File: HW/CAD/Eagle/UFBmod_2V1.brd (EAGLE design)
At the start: 98.4 x 89.5 mm, 204 parts, among them J1411 ABRACON_ARJE-0034, T0551 MMBT2222, U0501 MIDAS_MCCOG21605B6W-FPTLWI, U0601 MAX5217, U0701 AT86RF215-ZU, U0711 ASVTX-13-D-26.000MHZ-I05-T, U0811 PE4259, U0821 RFX1010, U0881 B39871B3440U410, U0911 FT232HL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

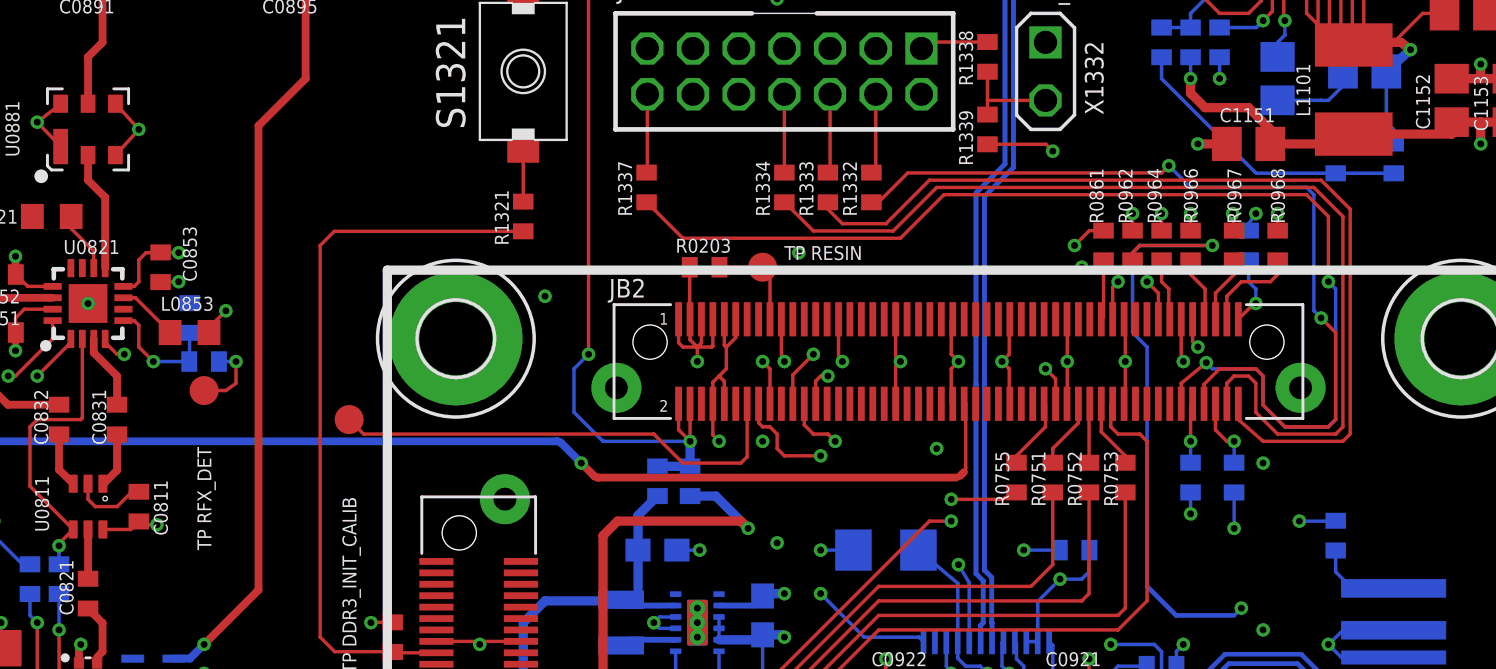
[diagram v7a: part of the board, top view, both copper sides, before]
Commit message: HW_2V1 - CAD/Eagle - missing polygone isles connected
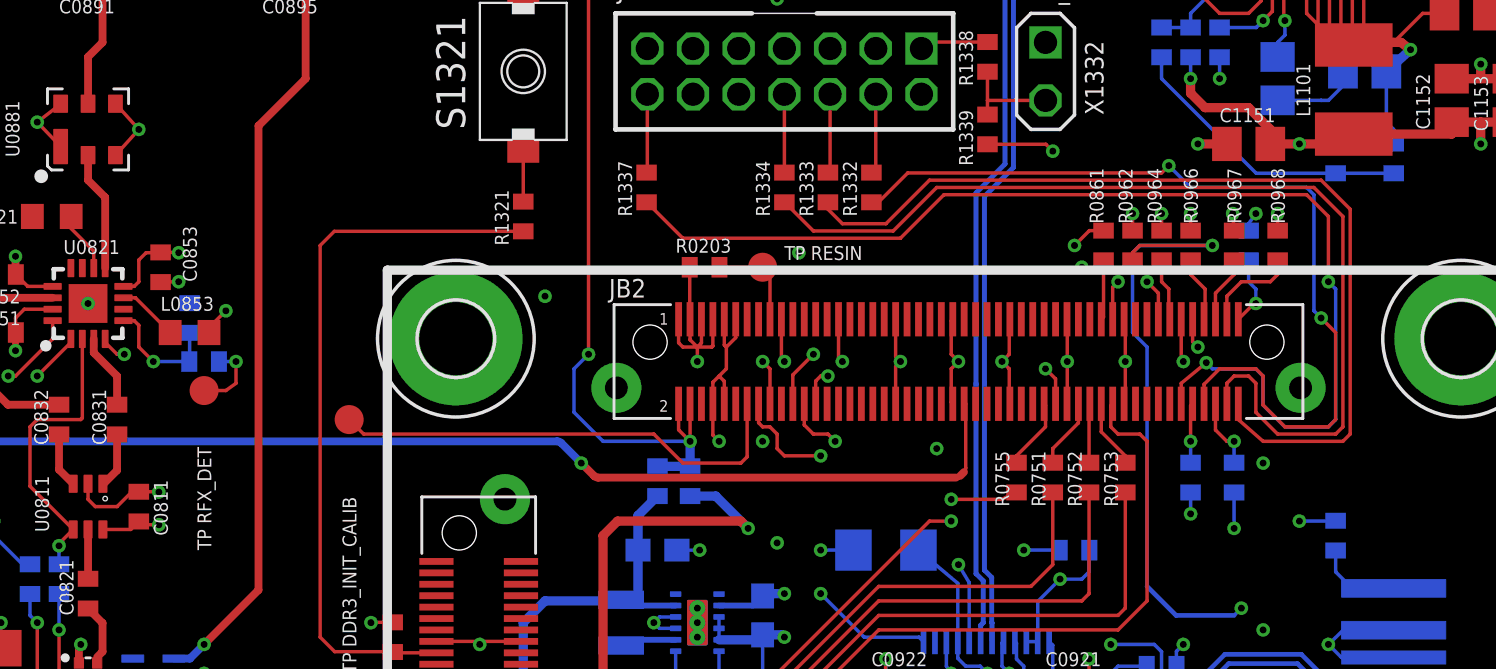
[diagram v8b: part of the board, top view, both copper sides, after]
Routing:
- net +3V3: track 98.2 -> 125.0 mm, vias 21 -> 22
- net GND: track 241.2 -> 242.1 mm, vias 83 -> 84
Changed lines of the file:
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@@
 <layer number="21" name="tPlace" color="7" fill="1" visible="yes" active="yes"/>
 <layer number="22" name="bPlace" color="7" fill="1" visible="yes" active="yes"/>
-<layer number="23" name="tOrigins" color="15" fill="1" visible="yes" active="yes"/>
-<layer number="24" name="bOrigins" color="15" fill="1" visible="yes" active="yes"/>
+<layer number="23" name="tOrigins" color="15" fill="1" visible="no" active="yes"/>
+<layer number="24" name="bOrigins" color="15" fill="1" visible="no" active="yes"/>
 <layer number="25" name="tNames" color="7" fill="1" visible="yes" active="yes"/>
 <layer number="26" name="bNames" color="7" fill="1" visible="yes" active="yes"/>
 <layer number="27" name="tValues" color="7" fill="1" visible="no" active="yes"/>
 <layer number="28" name="bValues" color="7" fill="1" visible="no" active="yes"/>
-<layer number="29" name="tStop" color="7" fill="3" visible="no" active="yes"/>
-<layer number="30" name="bStop" color="7" fill="6" visible="no" active="yes"/>
+<layer number="29" name="tStop" color="7" fill="3" visible="yes" active="yes"/>
+<layer number="30" name="bStop" color="7" fill="6" visible="yes" active="yes"/>
 <layer number="31" name="tCream" color="7" fill="4" visible="no" active="yes"/>
 <layer number="32" name="bCream" color="7" fill="5" visible="no" active="yes"/>
@@
 <layer number="43" name="vRestrict" color="2" fill="10" visible="yes" active="yes"/>
 <layer number="44" name="Drills" color="7" fill="1" visible="no" active="yes"/>
-<layer number="45" name="Holes" color="7" fill="1" visible="no" active="yes"/>
-<layer number="46" name="Milling" color="3" fill="1" visible="no" active="yes"/>
+<layer number="45" name="Holes" color="7" fill="1" visible="yes" active="yes"/>
+<layer number="46" name="Milling" color="3" fill="1" visible="yes" active="yes"/>
 <layer number="47" name="Measures" color="13" fill="1" visible="no" active="yes"/>
 <layer number="48" name="Document" color="7" fill="1" visible="no" active="yes"/>
 <layer number="49" name="Reference" color="7" fill="1" visible="yes" active="yes"/>
 <layer number="50" name="dxf" color="7" fill="1" visible="no" active="no"/>
-<layer number="51" name="tDocu" color="14" fill="1" visible="no" active="yes"/>
-<layer number="52" name="bDocu" color="6" fill="1" visible="no" active="yes"/>
+<layer number="51" name="tDocu" color="14" fill="1" visible="yes" active="yes"/>
+<layer number="52" name="bDocu" color="6" fill="1" visible="yes" active="yes"/>
 <layer number="53" name="tGND_GNDA" color="7" fill="9" visible="no" active="no"/>
 <layer number="54" name="bGND_GNDA" color="1" fill="9" visible="no" active="no"/>
@@
 </elements>
 <signals>
-<signal name="GND" airwireshidden="yes">
+<signal name="GND">
 <contactref element="H1511" pad="B3,2"/>
 <contactref element="H1512" pad="B3,2"/>
@@
 <wire x1="68.58" y1="41.26" x2="68.595" y2="41.26" width="0.1524" layer="16"/>
 <wire x1="68.595" y1="41.26" x2="69.5325" y2="40.3225" width="0.1524" layer="16"/>
-<wire x1="17.78" y1="55.61" x2="19.05" y2="61.2775" width="0" layer="19" extent="1-1"/>
+<via x="20.8788" y="55.245" extent="1-16" drill="0.3"/>
+<wire x1="20.0025" y1="55.26" x2="20.8788" y2="55.26" width="0.1524" layer="1"/>
+<wire x1="20.8788" y1="55.26" x2="20.8788" y2="55.245" width="0.1524" layer="1"/>
 </signal>
-<signal name="+3V3" airwireshidden="yes">
+<signal name="+3V3">
 <contactref element="L0703" pad="1"/>
 <contactref element="L0704" pad="1"/>
@@
 <wire x1="14.605" y1="62.865" x2="14.605" y2="62.245" width="0.1524" layer="1"/>
 <wire x1="14.605" y1="62.245" x2="14.62" y2="62.23" width="0.1524" layer="1"/>
-<via x="20.79625" y="53.81625" extent="1-16" drill="0.3"/>
+<via x="20.8788" y="53.81625" extent="1-16" drill="0.3"/>
 <wire x1="20.0025" y1="53.96" x2="20.14625" y2="53.81625" width="0.15" layer="1"/>
-<wire x1="20.14625" y1="53.81625" x2="20.79625" y2="53.81625" width="0.15" layer="1"/>
+<wire x1="20.14625" y1="53.81625" x2="20.8788" y2="53.81625" width="0.15" layer="1"/>
 <contactref element="L0853" pad="1"/>
 <contactref element="C0501" pad="1"/>
@@
 <wire x1="73.18375" y1="70.91625" x2="77.47" y2="70.91625" width="0.4064" layer="1"/>
 <wire x1="77.47" y1="70.91625" x2="77.47" y2="71.44" width="0.4064" layer="1"/>
-<wire x1="69.53" y1="70.485" x2="73.18375" y2="70.485" width="0.4064" layer="1"/>
+<wire x1="69.53" y1="70.485" x2="70.8025" y2="70.485" width="0.4064" layer="1"/>
+<wire x1="70.8025" y1="70.485" x2="73.18375" y2="70.485" width="0.4064" layer="1"/>
 <wire x1="73.18375" y1="70.485" x2="73.18375" y2="70.91625" width="0.4064" layer="1"/>
 <via x="78.74" y="70.485" extent="1-16" drill="0.3"/>
@@
 <wire x1="44.1175" y1="65.0875" x2="44.1175" y2="62.81" width="0.1524" layer="1"/>
 <wire x1="44.1175" y1="62.81" x2="44.13" y2="62.81" width="0.1524" layer="1"/>
-<wire x1="73.18375" y1="70.485" x2="72.39" y2="70.5" width="0" layer="19" extent="1-16"/>
-<wire x1="50.18" y1="43.815" x2="47.3075" y2="47.3075" width="0" layer="19" extent="16-16"/>
-<wire x1="67.6275" y1="42.545" x2="52.9" y2="43.15" width="0" layer="19" extent="16-16"/>
+<wire x1="51.1175" y1="43.815" x2="48.26" y2="46.6725" width="0.1524" layer="3"/>
+<wire x1="48.26" y1="46.6725" x2="48.26" y2="48.895" width="0.1524" layer="3"/>
+<wire x1="67.6275" y1="42.545" x2="66.675" y2="41.5925" width="0.1524" layer="2"/>
+<wire x1="66.675" y1="41.5925" x2="64.4525" y2="41.5925" width="0.1524" layer="2"/>
+<wire x1="64.4525" y1="41.5925" x2="63.1825" y2="40.3225" width="0.1524" layer="2"/>
+<wire x1="63.1825" y1="40.3225" x2="54.9275" y2="40.3225" width="0.1524" layer="2"/>
+<wire x1="54.9275" y1="40.3225" x2="51.435" y2="43.815" width="0.1524" layer="2"/>
+<wire x1="51.435" y1="43.815" x2="51.1175" y2="43.815" width="0.1524" layer="2"/>
+<via x="70.8025" y="70.485" extent="1-16" drill="0.3"/>
+<wire x1="70.8025" y1="70.485" x2="72.39" y2="70.485" width="0.1524" layer="16"/>
+<wire x1="72.39" y1="70.5" x2="72.39" y2="70.485" width="0.1524" layer="16"/>
 </signal>
 <signal name="P$8">
@@
 <wire x1="25.7175" y1="36.83" x2="25.55875" y2="36.83" width="0.1524" layer="3"/>
 </signal>
-<signal name="TRX_AVSS" airwireshidden="yes">
+<signal name="TRX_AVSS">
 <contactref element="L0701" pad="2"/>
 <contactref element="U0701" pad="45"/>
@@
 </polygon>
 </signal>
-<signal name="TRX_EVDD" airwireshidden="yes">
+<signal name="TRX_EVDD">
 <contactref element="L0704" pad="2"/>
 <contactref element="U0701" pad="46"/>
